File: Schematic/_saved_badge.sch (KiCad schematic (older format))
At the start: 50 parts, among them J1 Left2, J10 USB_B_Micro, J11 Penny2, J12 Penny1, J13 Penny0, J14 Power, J15 Right5, J4 Serial, J5 Penny3, J6 Right1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

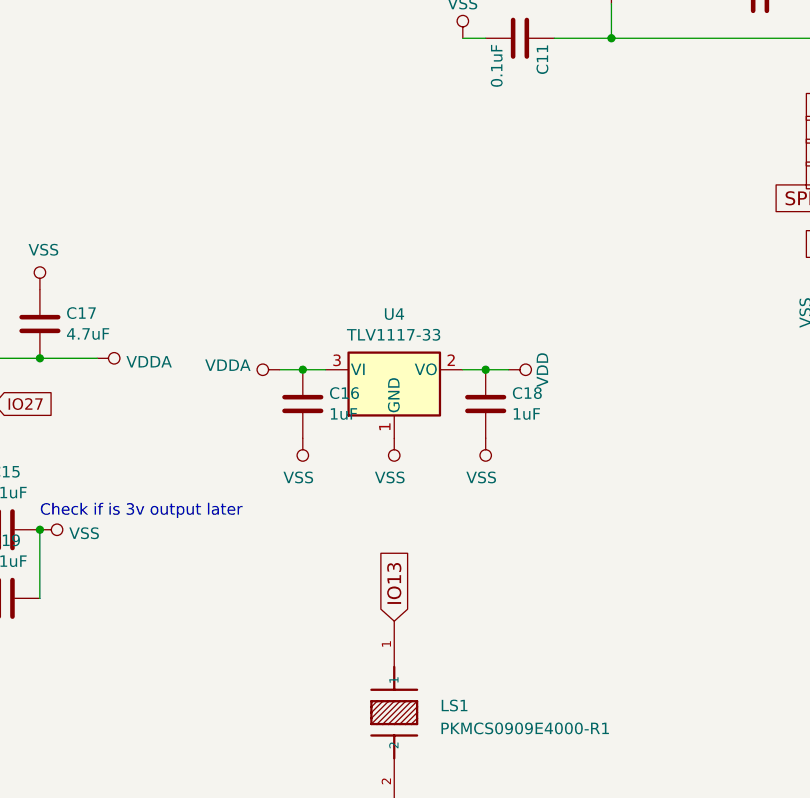
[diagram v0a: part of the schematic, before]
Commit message: Added charging hardware
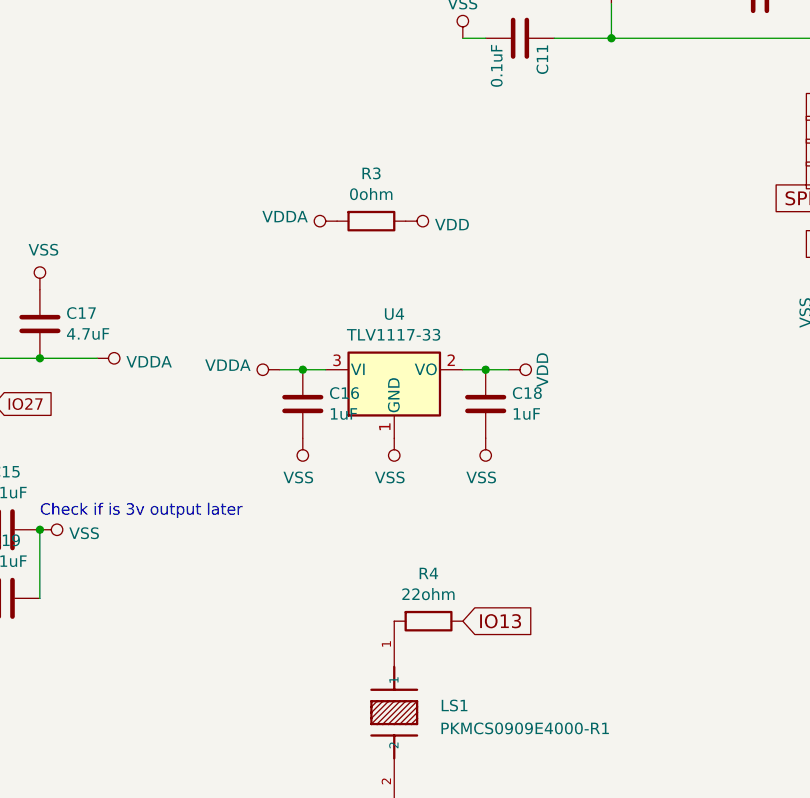
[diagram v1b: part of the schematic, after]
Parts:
- added R3: 0ohm, Resistors_SMD:R_0805_HandSoldering, symbol badge-rescue:R
- added R4: 22ohm, Resistors_SMD:R_0805_HandSoldering, symbol badge-rescue:R
- J8: footprint (none) -> Pin_Headers:Pin_Header_Straight_1x05_Pitch2.54mm
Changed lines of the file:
@@
 F 0 "J8" H 2900 3800 50  0000 C CNN
 F 1 "Right3" H 2900 3200 50  0000 C CNN
-F 2 "" H 2900 3500 50  0001 C CNN
+F 2 "Pin_Headers:Pin_Header_Straight_1x05_Pitch2.54mm" H 2900 3500 50  0001 C CNN
 F 3 "" H 2900 3500 50  0001 C CNN
 	1    2900 3500
@@
 	1    0    0    -1
 $EndComp
-Text GLabel 5700 6400 1    60   Input ~ 0
+Text GLabel 6000 6400 2    60   Input ~ 0
 IO13
 $Comp
@@
 NoConn ~ 7800 4050
 NoConn ~ 7800 4650
+$Comp
+L badge-rescue:R R3
+U 1 1 5C3808AE
+P 5600 4650
+F 0 "R3" V 5393 4650 50  0000 C CNN
+F 1 "0ohm" V 5484 4650 50  0000 C CNN
+F 2 "Resistors_SMD:R_0805_HandSoldering" V 5530 4650 50  0001 C CNN
+F 3 "" H 5600 4650 50  0001 C CNN
+	1    5600 4650
+	0    1    1    0
+$EndComp
+$Comp
+L badge-rescue:R R4
+U 1 1 5C3809AF
+P 5850 6400
+F 0 "R4" V 5643 6400 50  0000 C CNN
+F 1 "22ohm" V 5734 6400 50  0000 C CNN
+F 2 "Resistors_SMD:R_0805_HandSoldering" V 5780 6400 50  0001 C CNN
+F 3 "" H 5850 6400 50  0001 C CNN
+	1    5850 6400
+	0    1    1    0
+$EndComp
+$Comp
+L power:VDDA #PWR031
+U 1 1 5C380B3D
+P 5450 4650
+F 0 "#PWR031" H 5450 4500 50  0001 C CNN
+F 1 "VDDA" V 5468 4778 50  0000 L CNN
+F 2 "" H 5450 4650 50  0001 C CNN
+F 3 "" H 5450 4650 50  0001 C CNN
+	1    5450 4650
+	0    -1   -1   0
+$EndComp
+$Comp
+L power:VDD #PWR032
+U 1 1 5C380CD6
+P 5750 4650
+F 0 "#PWR032" H 5750 4500 50  0001 C CNN
+F 1 "VDD" V 5767 4778 50  0000 L CNN
+F 2 "" H 5750 4650 50  0001 C CNN
+F 3 "" H 5750 4650 50  0001 C CNN
+	1    5750 4650
+	0    1    1    0
+$EndComp
 $EndSCHEMATC
